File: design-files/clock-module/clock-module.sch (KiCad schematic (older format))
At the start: 32 parts, among them J101 Jack-DC, Q101 2N6491, SW101 SW_Push, SW102 SW_SPDT, SW103 SW_SPDT, U101 NE555P, U102 NE555P, U103 NE555P, U104 74HCT00, U105 74HCT00

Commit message: Update the clock module with the DC jack the boards will use.
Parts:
- removed J101: Jack-DC, symbol Connector:Jack-DC
- added J101: CUI_PJ-097BH-5_5-2_5mm-5A, jrt-Connectors:CUI_PJ-097BH-5_5-2_5mm-5A, symbol jrt-Connectors:CUI_PJ-097BH-5_5-2_5mm-5A
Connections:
- net +5V: now also J101.1
- net GND: now also J101.2
- no-connect marks 3 -> 4
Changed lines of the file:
@@
-$EndComp
-$Comp
-L Connector:Jack-DC J101
-U 1 1 61CA2FAF
-P 4000 6050
-F 0 "J101" H 4057 6375 50  0000 C CNN
-F 1 "Jack-DC" H 4057 6284 50  0000 C CNN
-F 2 "" H 4050 6010 50  0001 C CNN
-F 3 "~" H 4050 6010 50  0001 C CNN
-	1    4000 6050
-	1    0    0    -1
-$EndComp
-$Comp
-L power:+5V #PWR?
-U 1 1 61CA55F6
-P 4300 5950
-F 0 "#PWR?" H 4300 5800 50  0001 C CNN
-F 1 "+5V" V 4315 6078 50  0000 L CNN
-F 2 "" H 4300 5950 50  0001 C CNN
-F 3 "" H 4300 5950 50  0001 C CNN
-	1    4300 5950
-	0    1    1    0
-$EndComp
-$Comp
-L power:GND #PWR?
-U 1 1 61CA63D1
-P 4300 6150
-F 0 "#PWR?" H 4300 5900 50  0001 C CNN
-F 1 "GND" V 4305 6022 50  0000 R CNN
-F 2 "" H 4300 6150 50  0001 C CNN
-F 3 "" H 4300 6150 50  0001 C CNN
-	1    4300 6150
-	0    -1   -1   0
 $EndComp
 $Comp
@@
 Wire Wire Line
 	1700 6050 1850 6050
+$Comp
+L jrt-Connectors:CUI_PJ-097BH-5_5-2_5mm-5A J101
+U 1 1 6409DB36
+P 4000 6300
+F 0 "J101" H 4058 6715 50  0000 C CNN
+F 1 "CUI_PJ-097BH-5_5-2_5mm-5A" H 4058 6624 50  0000 C CNN
+F 2 "jrt-Connectors:CUI_PJ-097BH-5_5-2_5mm-5A" H 4200 6200 50  0001 C CNN
+F 3 "" H 4200 6200 50  0001 C CNN
+	1    4000 6300
+	1    0    0    -1
+$EndComp
+$Comp
+L power:+5V #PWR?
+U 1 1 640A04F3
+P 4450 6150
+F 0 "#PWR?" H 4450 6000 50  0001 C CNN
+F 1 "+5V" V 4465 6278 50  0000 L CNN
+F 2 "" H 4450 6150 50  0001 C CNN
+F 3 "" H 4450 6150 50  0001 C CNN
+	1    4450 6150
+	0    1    1    0
+$EndComp
+$Comp
+L power:GND #PWR?
+U 1 1 640A13FE
+P 4450 6450
+F 0 "#PWR?" H 4450 6200 50  0001 C CNN
+F 1 "GND" V 4455 6322 50  0000 R CNN
+F 2 "" H 4450 6450 50  0001 C CNN
+F 3 "" H 4450 6450 50  0001 C CNN
+	1    4450 6450
+	0    -1   -1   0
+$EndComp
+NoConn ~ 4450 6300
 $EndSCHEMATC

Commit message: Add footprints to the pots and switches on the clock module.
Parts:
- RV101: footprint (none) -> jrt-Potentiometers:Potentiometer_Alpha_RV09AF-40_vert
- SW101: footprint (none) -> Button_Switch_THT:SW_TH_Tactile_Omron_B3F-10xx
- SW102, SW103: footprint (none) -> jrt-Switches:NKK_BB16AP
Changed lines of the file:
@@
 F 0 "RV101" H 3340 2254 50  0000 R CNN
 F 1 "1M" H 3340 2345 50  0000 R CNN
-F 2 "" H 3400 2300 50  0001 C CNN
+F 2 "jrt-Potentiometers:Potentiometer_Alpha_RV09AF-40_vert" H 3400 2300 50  0001 C CNN
 F 3 "~" H 3400 2300 50  0001 C CNN
 F 4 "317-2090F-1M" H 3400 2300 50  0001 C CNN "Mouser"
@@
 F 0 "SW101" H 4100 1800 50  0000 C CNN
 F 1 "SW_Push" H 4100 1700 50  0000 C CNN
-F 2 "" H 4100 2100 50  0001 C CNN
+F 2 "Button_Switch_THT:SW_TH_Tactile_Omron_B3F-10xx" H 4100 2100 50  0001 C CNN
 F 3 "~" H 4100 2100 50  0001 C CNN
 F 4 "179-TS0266150BK100SC" H 4100 1900 50  0001 C CNN "Mouser"
@@
 F 0 "SW102" H 6650 2685 50  0000 C CNN
 F 1 "SW_SPDT" H 6650 2594 50  0000 C CNN
-F 2 "" H 6650 2400 50  0001 C CNN
+F 2 "jrt-Switches:NKK_BB16AP" H 6650 2400 50  0001 C CNN
 F 3 "~" H 6650 2400 50  0001 C CNN
 F 4 "633-BB16APFA" H 6650 2400 50  0001 C CNN "Mouser"
@@
 F 0 "SW103" H 1500 6435 50  0000 C CNN
 F 1 "SW_SPDT" H 1500 6344 50  0000 C CNN
-F 2 "" H 1500 6150 50  0001 C CNN
+F 2 "jrt-Switches:NKK_BB16AP" H 1500 6150 50  0001 C CNN
 F 3 "~" H 1500 6150 50  0001 C CNN
 F 4 "633-BB16APFA" H 1500 6150 50  0001 C CNN "Mouser"

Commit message: Add footprints to the 'lytics on the clock module.
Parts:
- C103, C111: footprint (none) -> Capacitor_THT:CP_Radial_D8.0mm_P5.00mm; Mouser (none) -> 667-ECA-2VM010B
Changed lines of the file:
@@
 $EndComp
 $Comp
-L power:GND #PWR?
+L power:GND #PWR0101
 U 1 1 61B8C11C
 P 2500 1750
-F 0 "#PWR?" H 2500 1500 50  0001 C CNN
+F 0 "#PWR0101" H 2500 1500 50  0001 C CNN
 F 1 "GND" H 2505 1577 50  0000 C CNN
 F 2 "" H 2500 1750 50  0001 C CNN
@@
 $EndComp
 $Comp
-L power:GND #PWR?
+L power:GND #PWR0102
 U 1 1 61B8CB89
 P 5400 1750
-F 0 "#PWR?" H 5400 1500 50  0001 C CNN
+F 0 "#PWR0102" H 5400 1500 50  0001 C CNN
 F 1 "GND" H 5405 1577 50  0000 C CNN
 F 2 "" H 5400 1750 50  0001 C CNN
@@
 $EndComp
 $Comp
-L power:GND #PWR?
+L power:GND #PWR0103
 U 1 1 61B8CDCC
 P 8250 1750
-F 0 "#PWR?" H 8250 1500 50  0001 C CNN
+F 0 "#PWR0103" H 8250 1500 50  0001 C CNN
 F 1 "GND" H 8255 1577 50  0000 C CNN
 F 2 "" H 8250 1750 50  0001 C CNN
@@
 $EndComp
 $Comp
-L power:GND #PWR?
+L power:GND #PWR0104
 U 1 1 61B8D4F5
 P 7150 3100
-F 0 "#PWR?" H 7150 2850 50  0001 C CNN
+F 0 "#PWR0104" H 7150 2850 50  0001 C CNN
 F 1 "GND" H 7155 2927 50  0000 C CNN
 F 2 "" H 7150 3100 50  0001 C CNN
@@
 F 0 "C103" H 1841 2946 50  0000 L CNN
 F 1 "1µF" H 1841 2855 50  0000 L CNN
-F 2 "" H 1750 2900 50  0001 C CNN
+F 2 "Capacitor_THT:CP_Radial_D8.0mm_P5.00mm" H 1750 2900 50  0001 C CNN
 F 3 "~" H 1750 2900 50  0001 C CNN
+F 4 "667-ECA-2VM010B" H 1750 2900 50  0001 C CNN "Mouser"
 	1    1750 2900
 	1    0    0    -1
@@
 	1350 2300 1350 2800
 $Comp
-L power:GND #PWR?
+L power:GND #PWR0105
 U 1 1 61B96824
 P 1750 3100
-F 0 "#PWR?" H 1750 2850 50  0001 C CNN
+F 0 "#PWR0105" H 1750 2850 50  0001 C CNN
 F 1 "GND" H 1755 2927 50  0000 C CNN
 F 2 "" H 1750 3100 50  0001 C CNN
@@
 $EndComp
 $Comp
-L power:GND #PWR?
+L power:GND #PWR0106
 U 1 1 61BAA633
 P 4300 3100
-F 0 "#PWR?" H 4300 2850 50  0001 C CNN
+F 0 "#PWR0106" H 4300 2850 50  0001 C CNN
 F 1 "GND" H 4305 2927 50  0000 C CNN
 F 2 "" H 4300 3100 50  0001 C CNN
@@
 $EndComp
 $Comp
-L power:VCC #PWR?
+L power:VCC #PWR0107
 U 1 1 61C29F7B
 P 2150 1550
-F 0 "#PWR?" H 2150 1400 50  0001 C CNN
+F 0 "#PWR0107" H 2150 1400 50  0001 C CNN
 F 1 "VCC" H 2165 1723 50  0000 C CNN
 F 2 "" H 2150 1550 50  0001 C CNN
@@
 $EndComp
 $Comp
-L power:VCC #PWR?
+L power:VCC #PWR0108
 U 1 1 61C2A946
 P 5050 1550
-F 0 "#PWR?" H 5050 1400 50  0001 C CNN
+F 0 "#PWR0108" H 5050 1400 50  0001 C CNN
 F 1 "VCC" H 5065 1723 50  0000 C CNN
 F 2 "" H 5050 1550 50  0001 C CNN
@@
 $EndComp
 $Comp
-L power:VCC #PWR?
+L power:VCC #PWR0109
 U 1 1 61C2AF89
 P 7900 1500
-F 0 "#PWR?" H 7900 1350 50  0001 C CNN
+F 0 "#PWR0109" H 7900 1350 50  0001 C CNN
 F 1 "VCC" H 7915 1673 50  0000 C CNN
 F 2 "" H 7900 1500 50  0001 C CNN
@@
 $EndComp
 $Comp
-L power:GND #PWR?
+L power:GND #PWR0110
 U 1 1 61C493C1
 P 7150 4950
-F 0 "#PWR?" H 7150 4700 50  0001 C CNN
+F 0 "#PWR0110" H 7150 4700 50  0001 C CNN
 F 1 "GND" H 7155 4777 50  0000 C CNN
 F 2 "" H 7150 4950 50  0001 C CNN
@@
 $EndComp
 $Comp
-L power:GND #PWR?
+L power:GND #PWR0111
 U 1 1 61C49C28
 P 8100 4950
-F 0 "#PWR?" H 8100 4700 50  0001 C CNN
+F 0 "#PWR0111" H 8100 4700 50  0001 C CNN
 F 1 "GND" H 8105 4777 50  0000 C CNN
 F 2 "" H 8100 4950 50  0001 C CNN
@@
 	8100 3800 8500 3800
 $Comp
-L power:GND #PWR?
+L power:GND #PWR0112
 U 1 1 61C537B0
 P 7550 4000
-F 0 "#PWR?" H 7550 3750 50  0001 C CNN
+F 0 "#PWR0112" H 7550 3750 50  0001 C CNN
 F 1 "GND" H 7555 3827 50  0000 C CNN
 F 2 "" H 7550 4000 50  0001 C CNN
@@
 $EndComp
 $Comp
-L power:GND #PWR?
+L power:GND #PWR0113
 U 1 1 61C543B9
 P 8500 4000
-F 0 "#PWR?" H 8500 3750 50  0001 C CNN
+F 0 "#PWR0113" H 8500 3750 50  0001 C CNN
 F 1 "GND" H 8505 3827 50  0000 C CNN
 F 2 "" H 8500 4000 50  0001 C CNN
@@
 $EndComp
 $Comp
-L power:VCC #PWR?
+L power:VCC #PWR0114
 U 1 1 61C54C1D
 P 7150 3800
-F 0 "#PWR?" H 7150 3650 50  0001 C CNN
+F 0 "#PWR0114" H 7150 3650 50  0001 C CNN
 F 1 "VCC" H 7165 3973 50  0000 C CNN
 F 2 "" H 7150 3800 50  0001 C CNN
@@
 Connection ~ 7150 3800
 $Comp
-L power:VCC #PWR?
+L power:VCC #PWR0115
 U 1 1 61C5546C
 P 8100 3800
-F 0 "#PWR?" H 8100 3650 50  0001 C CNN
+F 0 "#PWR0115" H 8100 3650 50  0001 C CNN
 F 1 "VCC" H 8115 3973 50  0000 C CNN
 F 2 "" H 8100 3800 50  0001 C CNN
@@
 $EndComp
 $Comp
-L power:GND #PWR?
+L power:GND #PWR0116
 U 1 1 61C5C4F5
 P 5800 3400
-F 0 "#PWR?" H 5800 3150 50  0001 C CNN
+F 0 "#PWR0116" H 5800 3150 50  0001 C CNN
 F 1 "GND" H 5805 3227 50  0000 C CNN
 F 2 "" H 5800 3400 50  0001 C CNN
@@
 $EndComp
 $Comp
-L power:+5V #PWR?
+L power:+5V #PWR0117
 U 1 1 61C7FDAF
 P 2150 5650
-F 0 "#PWR?" H 2150 5500 50  0001 C CNN
+F 0 "#PWR0117" H 2150 5500 50  0001 C CNN
 F 1 "+5V" H 2165 5823 50  0000 C CNN
 F 2 "" H 2150 5650 50  0001 C CNN
@@
 F 0 "C111" H 2491 6546 50  0000 L CNN
 F 1 "1µF" H 2491 6455 50  0000 L CNN
-F 2 "" H 2400 6500 50  0001 C CNN
+F 2 "Capacitor_THT:CP_Radial_D8.0mm_P5.00mm" H 2400 6500 50  0001 C CNN
 F 3 "~" H 2400 6500 50  0001 C CNN
+F 4 "667-ECA-2VM010B" H 2400 6500 50  0001 C CNN "Mouser"
 	1    2400 6500
 	1    0    0    -1
@@
 	2400 6250 2400 6400
 $Comp
-L power:VCC #PWR?
+L power:VCC #PWR0118
 U 1 1 61C909FA
 P 2750 6250
-F 0 "#PWR?" H 2750 6100 50  0001 C CNN
+F 0 "#PWR0118" H 2750 6100 50  0001 C CNN
 F 1 "VCC" V 2765 6378 50  0000 L CNN
 F 2 "" H 2750 6250 50  0001 C CNN
@@
 Connection ~ 2400 6250
 $Comp
-L power:GND #PWR?
+L power:GND #PWR0119
 U 1 1 61C95171
 P 2400 6600
-F 0 "#PWR?" H 2400 6350 50  0001 C CNN
+F 0 "#PWR0119" H 2400 6350 50  0001 C CNN
 F 1 "GND" H 2405 6427 50  0000 C CNN
 F 2 "" H 2400 6600 50  0001 C CNN
@@
 	1400 6600 1400 6700
 $Comp
-L power:GND #PWR?
+L power:GND #PWR0120
 U 1 1 61CA1414
 P 1400 6900
-F 0 "#PWR?" H 1400 6650 50  0001 C CNN
+F 0 "#PWR0120" H 1400 6650 50  0001 C CNN
 F 1 "GND" H 1405 6727 50  0000 C CNN
 F 2 "" H 1400 6900 50  0001 C CNN
@@
 $EndComp
 $Comp
-L power:+5V #PWR?
+L power:+5V #PWR0121
 U 1 1 640A04F3
 P 4450 6150
-F 0 "#PWR?" H 4450 6000 50  0001 C CNN
+F 0 "#PWR0121" H 4450 6000 50  0001 C CNN
 F 1 "+5V" V 4465 6278 50  0000 L CNN
 F 2 "" H 4450 6150 50  0001 C CNN
@@
 $EndComp
 $Comp
-L power:GND #PWR?
+L power:GND #PWR0122
 U 1 1 640A13FE
 P 4450 6450
-F 0 "#PWR?" H 4450 6200 50  0001 C CNN
+F 0 "#PWR0122" H 4450 6200 50  0001 C CNN
 F 1 "GND" V 4455 6322 50  0000 R CNN
 F 2 "" H 4450 6450 50  0001 C CNN

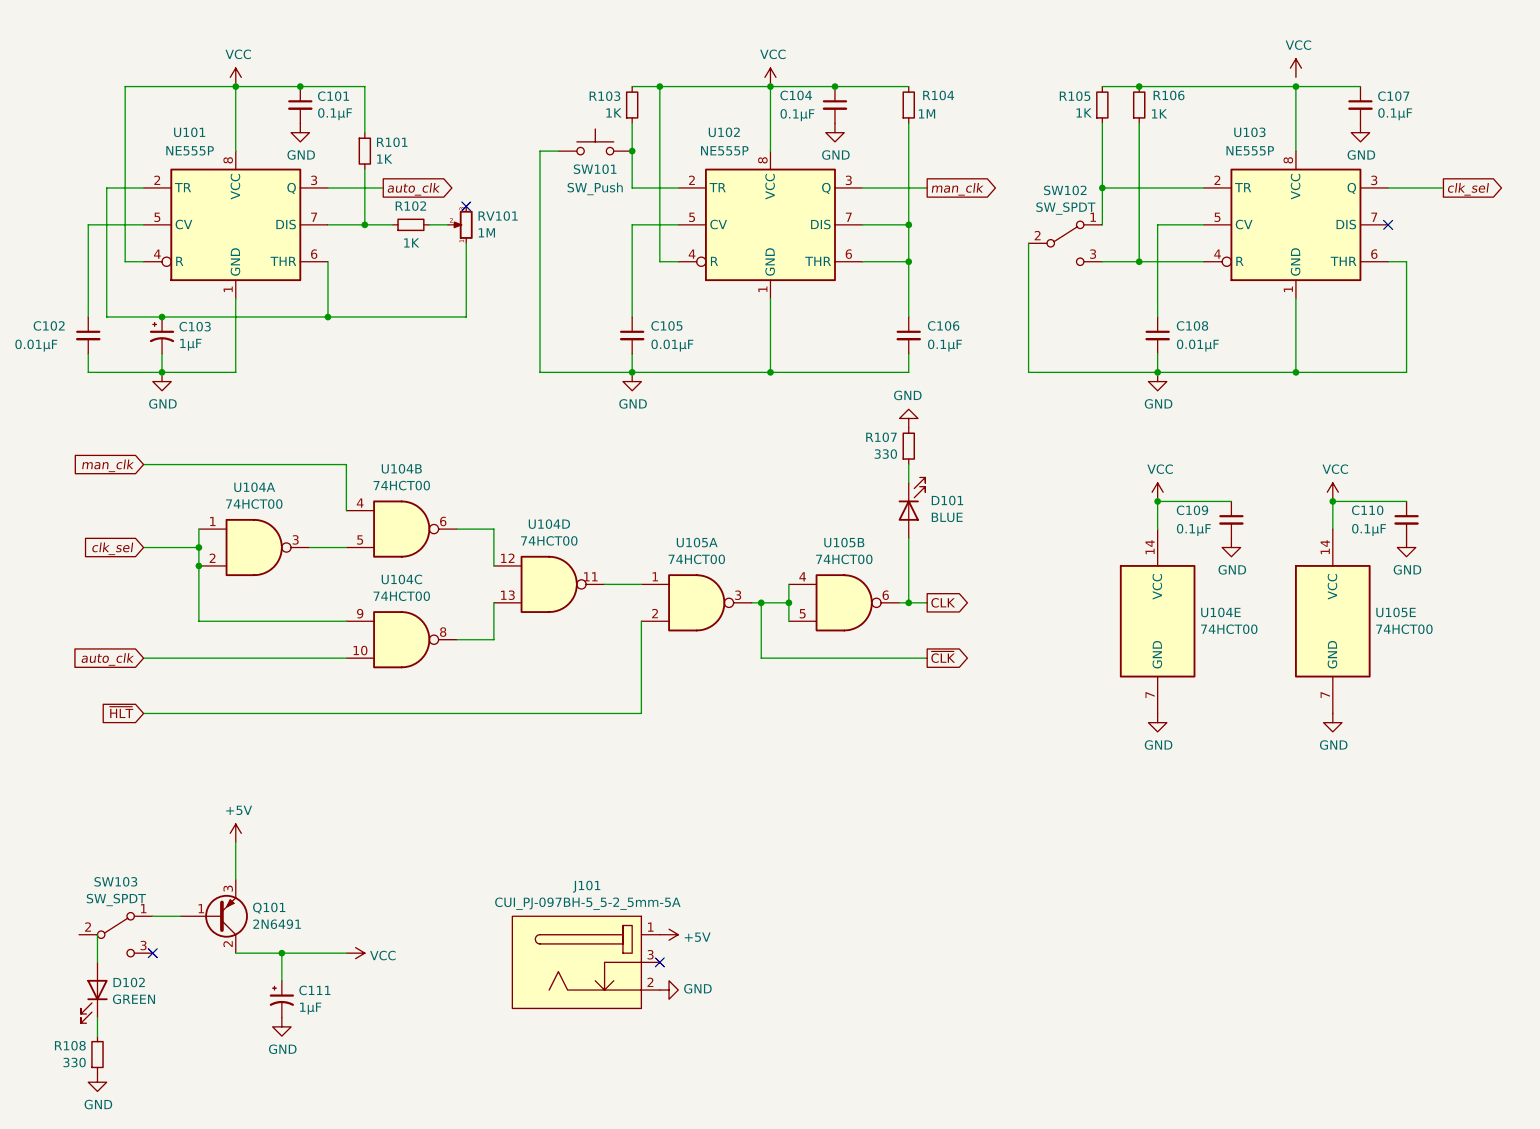
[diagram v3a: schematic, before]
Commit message: clock-module: 1- Remove ~CLK signal. there is no need to make that an output from    the clock module; only the control unit uses it. 2- Document the nominal frequency range for the auto clock.
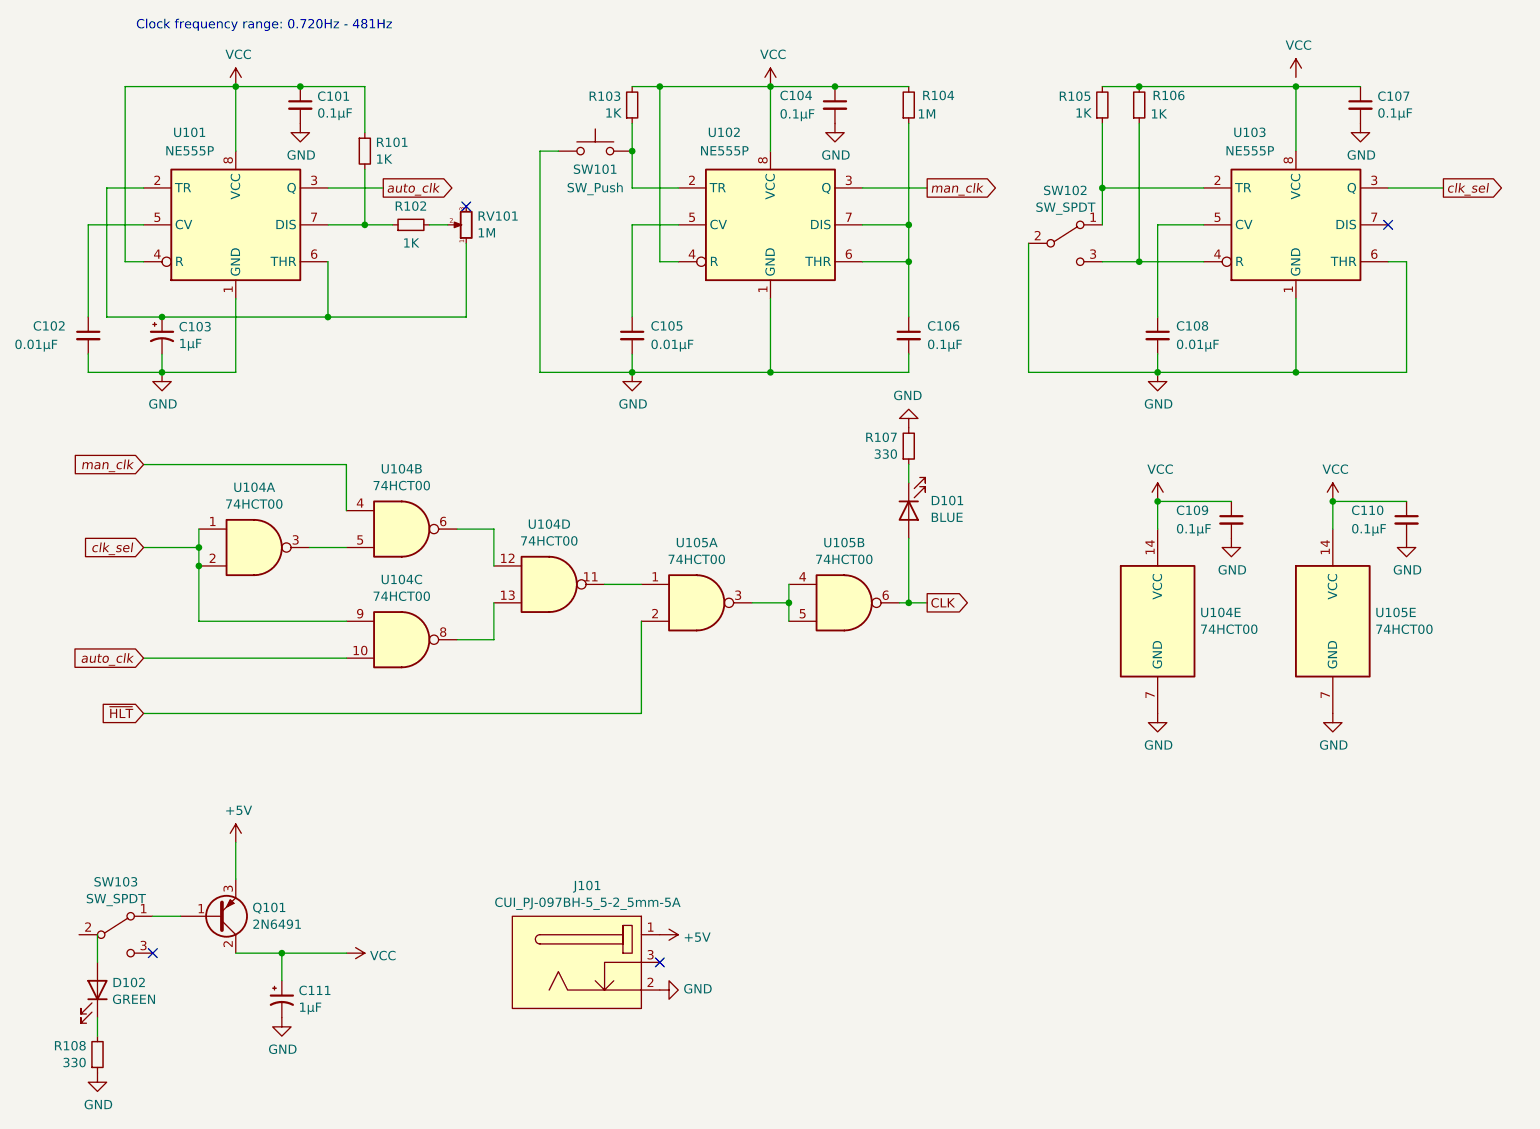
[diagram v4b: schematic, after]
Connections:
- net ~CLK: no longer names the net of U105.3, U105.4, U105.5
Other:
- note added: "Clock frequency range: 0.720Hz - 481Hz"
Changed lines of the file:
@@
 Wire Wire Line
 	5150 4250 5150 4350
-Wire Wire Line
-	4950 4350 5000 4350
 Connection ~ 5150 4350
 Wire Wire Line
@@
 Text GLabel 5900 4350 2    50   Output ~ 0
 CLK
-Text GLabel 5900 4650 2    50   Output ~ 0
-~CLK
-Wire Wire Line
-	5000 4350 5000 4650
-Wire Wire Line
-	5000 4650 5900 4650
-Connection ~ 5000 4350
-Wire Wire Line
-	5000 4350 5150 4350
 Wire Wire Line
 	5750 4350 5800 4350
@@
 $EndComp
 NoConn ~ 4450 6300
+Text Notes 3000 1250 2    50   ~ 0
+Clock frequency range: 0.720Hz - 481Hz
+Wire Wire Line
+	4950 4350 5150 4350
 $EndSCHEMATC
